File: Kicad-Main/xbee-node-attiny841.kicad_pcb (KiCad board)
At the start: 2 copper layers, 58.5 x 58.5 mm, 40 parts, among them P10 CONN_1, P11 CONN_1, P12 CONN_1, P13 CONN_1, P14 CONN_1, P15 CONN_1, P16 CONN_1, P17 CONN_1, P18 CONN_1, P19 CONN_1, P2 XBee Adaptor, P20 CONN_1, P3 Debug Adaptor, P7 CONN_1, P8 CONN_1, P9 CONN_1, Q2 MMBT3904, Q3 2N7002, U1 ATTINY841, U2 MAX952ESA, U3 TPS77033

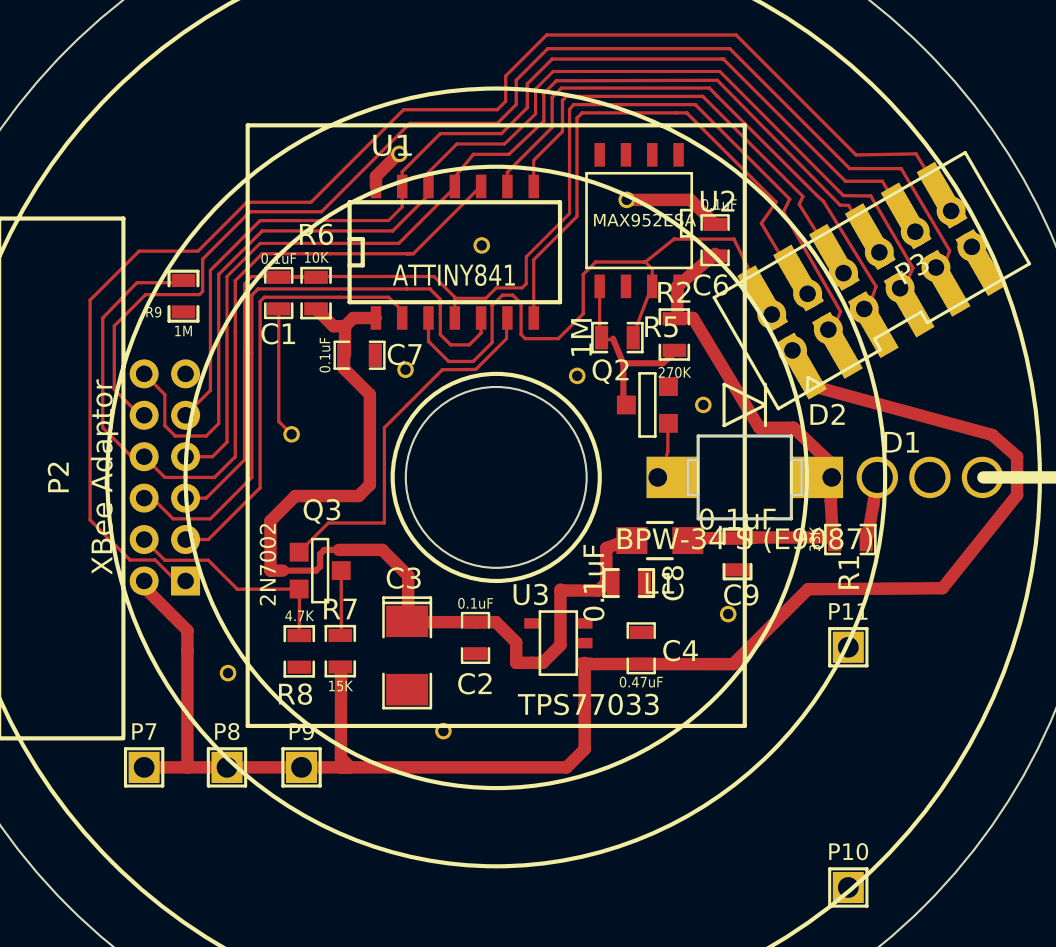
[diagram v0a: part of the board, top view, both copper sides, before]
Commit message: Update of Main PCB and generation of gerbers.
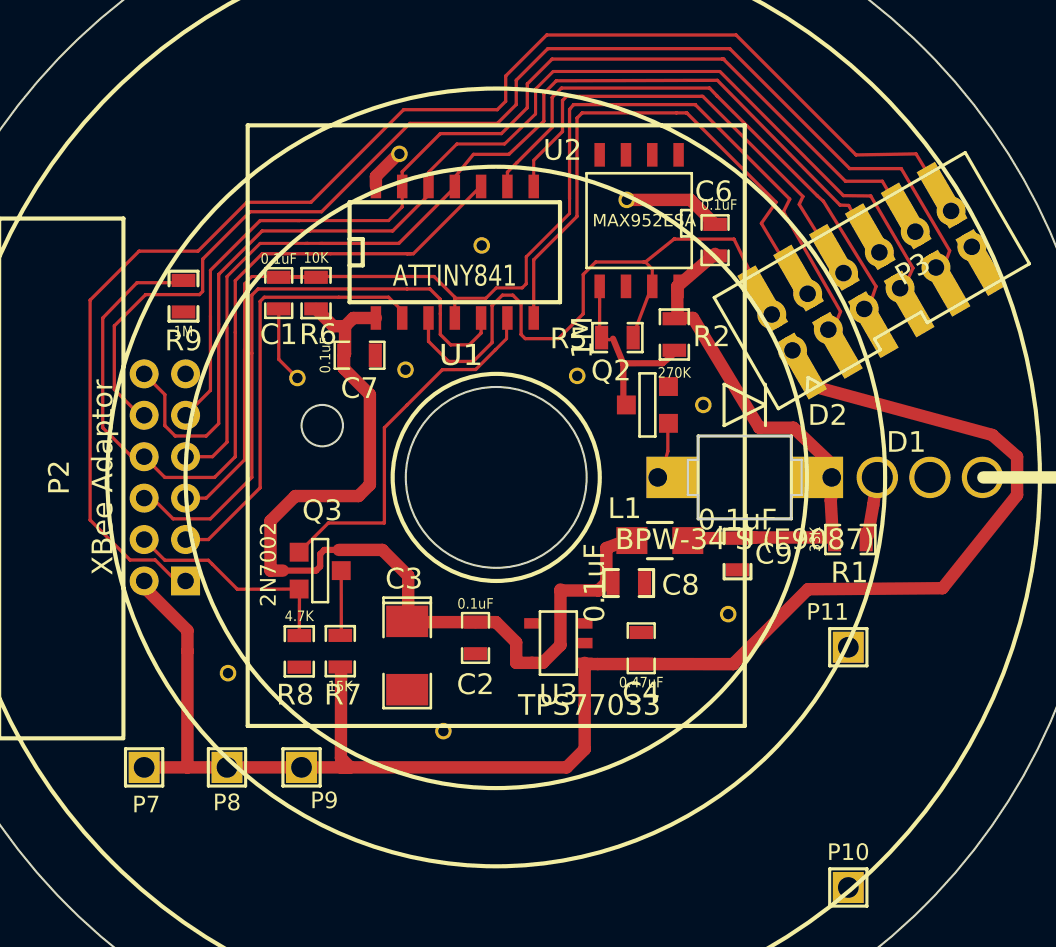
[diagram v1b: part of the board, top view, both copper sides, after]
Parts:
- moved P12 2.73 mm to (190.4, 95.2)
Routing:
- net GND: track 13.2 -> 10.6 mm
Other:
- outline, holes or cut-outs redrawn

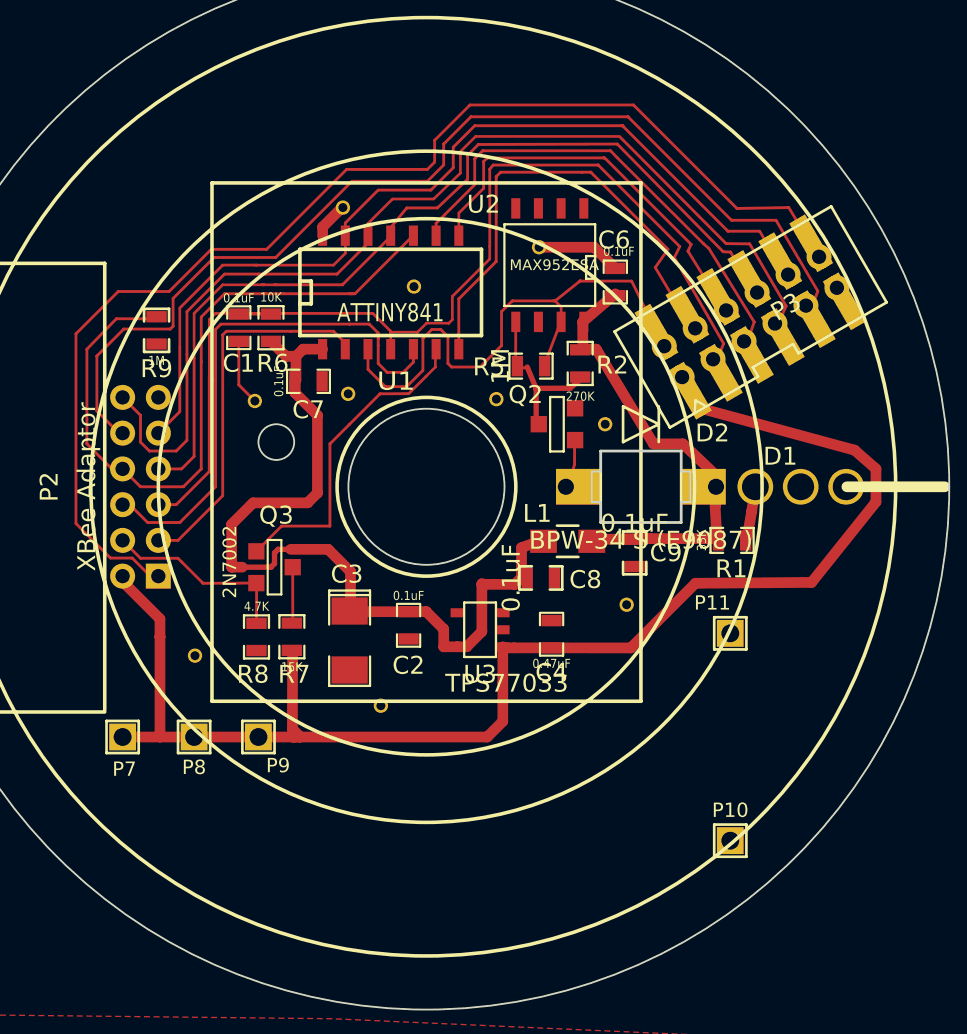
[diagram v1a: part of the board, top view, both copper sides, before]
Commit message: Update Main board PCB to modify battery monitor circuit.
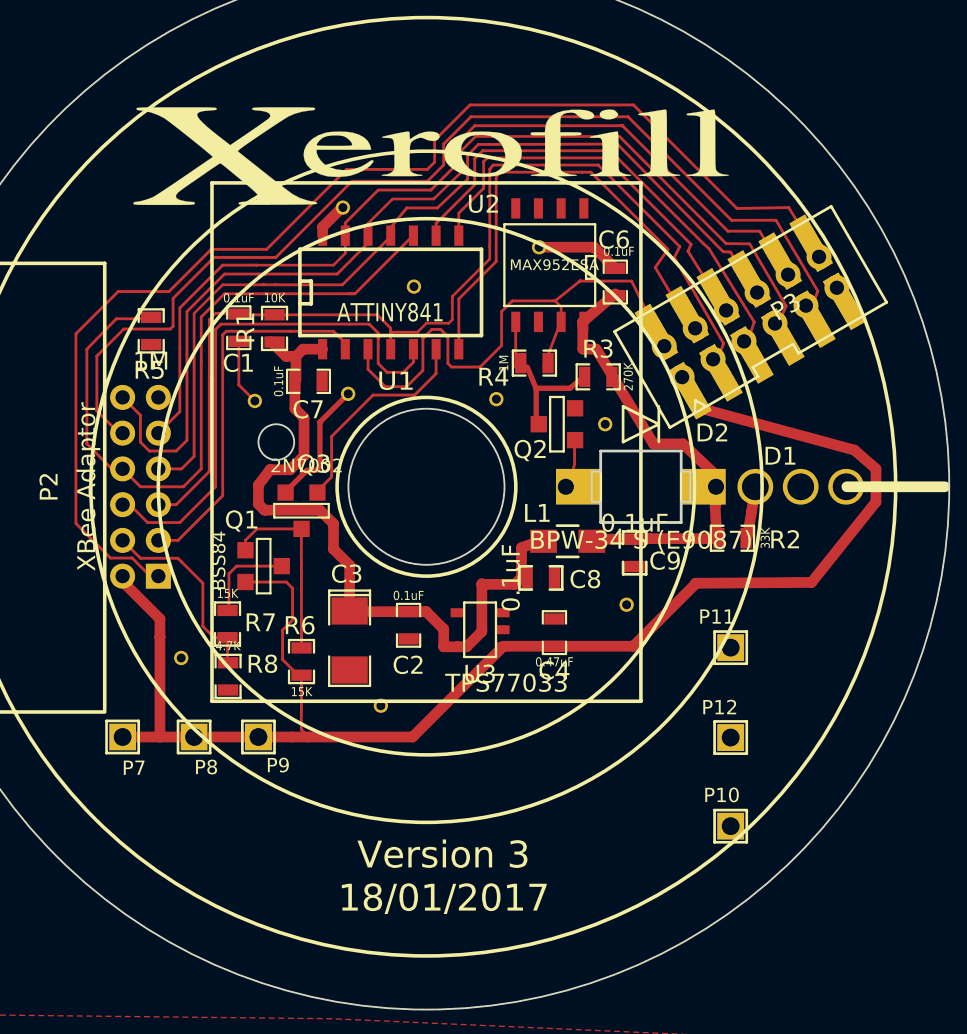
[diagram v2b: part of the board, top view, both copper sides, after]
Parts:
- removed R9: 1M, SMD_Packages:SMD-0603_r
- added G***: LOGO, PhotoDiode:Xerofill-Logo-Big, F.Cu at (200.2, 81.5)
- added P12: CONN_1, Connect:SIL-1, F.Cu at (217.0, 114.0)
- added Q1: BSS84, PhotoDiode:SOT23GDS, F.Cu at (190.9, 104.4)
- added R3: 270K, PhotoDiode:SM0603_Resistor, F.Cu at (209.6, 93.8)
- added R4: 1M, PhotoDiode:SM0603_Resistor, F.Cu at (206.0, 93.1)
- R1: value 33K -> 10K
- R2: value 270K -> 33K
- R6: value 10K -> 15K
- moved R1 28.2 mm to (191.5, 91.1), turned to 270 degrees
- moved R5 21.3 mm to (184.6, 91.3), turned to 90 degrees
- moved R6 18.8 mm to (193.0, 109.8), turned to 90 degrees
- moved R2 13.0 mm to (217.1, 102.9), turned to 0 degrees
- moved R7 3.67 mm to (188.9, 107.7), turned to 270 degrees
- moved Q3 3.50 mm to (193.0, 101.3), turned to 0 degrees
- moved R8 2.72 mm to (188.9, 110.6)
- moved P10 0.81 mm to (217.0, 119.0)
- moved P11 0.80 mm to (217.0, 109.0)
- moved P17 0.78 mm to (186.3, 109.6)
- moved C4 0.18 mm to (207.2, 108.2)
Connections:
- Q3 pad D: Net-(Q3-PadD) -> Net-(Q1-PadG)
- Q3 pad S: /VBatt -> GND
- R1 pad 1: /VDDA -> /Reset
- R1 pad 2: Net-(D1-Pad1) -> VDD
- R2 pad 2: Net-(Q2-Pad3) -> Net-(D1-Pad1)
- R5 pad 1: Net-(Q2-Pad3) -> GND
- R5 pad 2: /Count -> /Sleep-Rq
- R6 pad 1: /Reset -> /Battery
- R6 pad 2: VDD -> Net-(Q1-PadG)
- R7 pad 1: /Battery -> Net-(Q1-PadD)
- R7 pad 2: Net-(Q3-PadD) -> /VBatt
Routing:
- net Net-(Q1-PadG): track 0.00 -> 10.7 mm
- net GND: track 10.6 -> 17.9 mm
- net VDD: track 53.5 -> 47.0 mm
- net /PowerControl: track 18.1 -> 11.9 mm
- net Net-(Q1-PadD): track 0.00 -> 5.22 mm
- net Net-(Q3-PadD): track 3.25 -> 0.00 mm
- net /Reset: track 59.5 -> 57.9 mm
- net /Battery: track 85.6 -> 86.9 mm
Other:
- board text added: "Version 3 18/01/2017"

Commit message: Kicad-Main, Kicad-Mounts and Kicad-Testboard. Add a range of symbol and footprint libraries and repair some problems apparently due to randomized changes in Kicad repository libraries.
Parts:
- L1: value INDUCTOR_SMALL -> 100nH
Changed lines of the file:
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@@
     (links 99)
     (no_connects 4)
-    (area 162.31 68.7 242.200001 132.330001)
+    (area 170.699999 70.699999 229.300001 129.300001)
     (thickness 1.6)
     (drawings 29)
@@
   )
   (setup
-    (last_trace_width 0.3)
+    (last_trace_width 0.16)
     (user_trace_width 0.3)
     (user_trace_width 0.6)
@@
       (effects (font (size 1 1) (thickness 0.15)))
     )
-    (fp_text value INDUCTOR_SMALL (at 0 2.1 180) (layer F.Fab)
+    (fp_text value 100nH (at 0 2.1 180) (layer F.Fab)
       (effects (font (size 1 1) (thickness 0.15)))
     )
@@
   (segment (start 186.2 102) (end 184.4 102) (width 0.16) (layer F.Cu) (net 8))
   (segment (start 188.2 100) (end 186.2 102) (width 0.16) (layer F.Cu) (net 8))
-  (segment (start 192.121 100.324) (end 192.121 100.269) (width 0.3) (layer F.Cu) (net 9) (status C00000))
-  (segment (start 192.121 100.269) (end 193.31 99.08) (width 0.3) (layer F.Cu) (net 9) (status 400000))
+  (segment (start 193.82 99.08) (end 194.04 98.86) (width 0.3) (layer F.Cu) (net 9))
   (segment (start 193.31 99.08) (end 193.82 99.08) (width 0.3) (layer F.Cu) (net 9))
-  (segment (start 193.82 99.08) (end 194.04 98.86) (width 0.3) (layer F.Cu) (net 9))
+  (segment (start 192.121 100.324) (end 192.121 100.269) (width 0.3) (layer F.Cu) (net 9))
+  (segment (start 192.121 100.269) (end 193.31 99.08) (width 0.3) (layer F.Cu) (net 9))
   (segment (start 194.04 98.86) (end 194.04 96.38) (width 0.3) (layer F.Cu) (net 9))
-  (segment (start 194.04 96.38) (end 195.62 94.8) (width 0.3) (layer F.Cu) (net 9) (status 800000))
+  (segment (start 194.04 96.38) (end 195.62 94.8) (width 0.3) (layer F.Cu) (net 9))
   (segment (start 189.5 91.862) (end 189.5 94.3) (width 0.16) (layer F.Cu) (net 9))
   (segment (start 189.5 94.3) (end 190.4 95.2) (width 0.16) (layer F.Cu) (net 9))
@@
   (segment (start 194.19 85.464) (end 194.19 85.952) (width 0.6) (layer F.Cu) (net 9))
   (segment (start 194.19 85.952) (end 194.148 85.952) (width 0.15) (layer F.Cu) (net 9))
-  (segment (start 192.638 94.1) (end 192.638 95.628) (width 0.6) (layer F.Cu) (net 12) (status 400000))
+  (segment (start 192.638 94.1) (end 192.638 95.628) (width 0.6) (layer F.Cu) (net 12))
   (segment (start 192.37 99.05) (end 191.248125 99.05) (width 0.6) (layer F.Cu) (net 12))
   (segment (start 193.15 98.27) (end 192.37 99.05) (width 0.6) (layer F.Cu) (net 12))

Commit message: Minor tweaks on the PCBs ready to manufacture
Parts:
- added R9: 1M, PhotoDiode:SM0603_Resistor, F.Cu at (194.3, 96.5)
- moved P12 1.04 mm to (190.1, 94.2)
- moved P15 0.80 mm to (195.7, 94.0)
- moved P10 0.11 mm to (217.0, 119.1)
- moved P11 0.10 mm to (217.0, 108.9)
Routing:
- net /VDDA: track 30.3 -> 33.7 mm

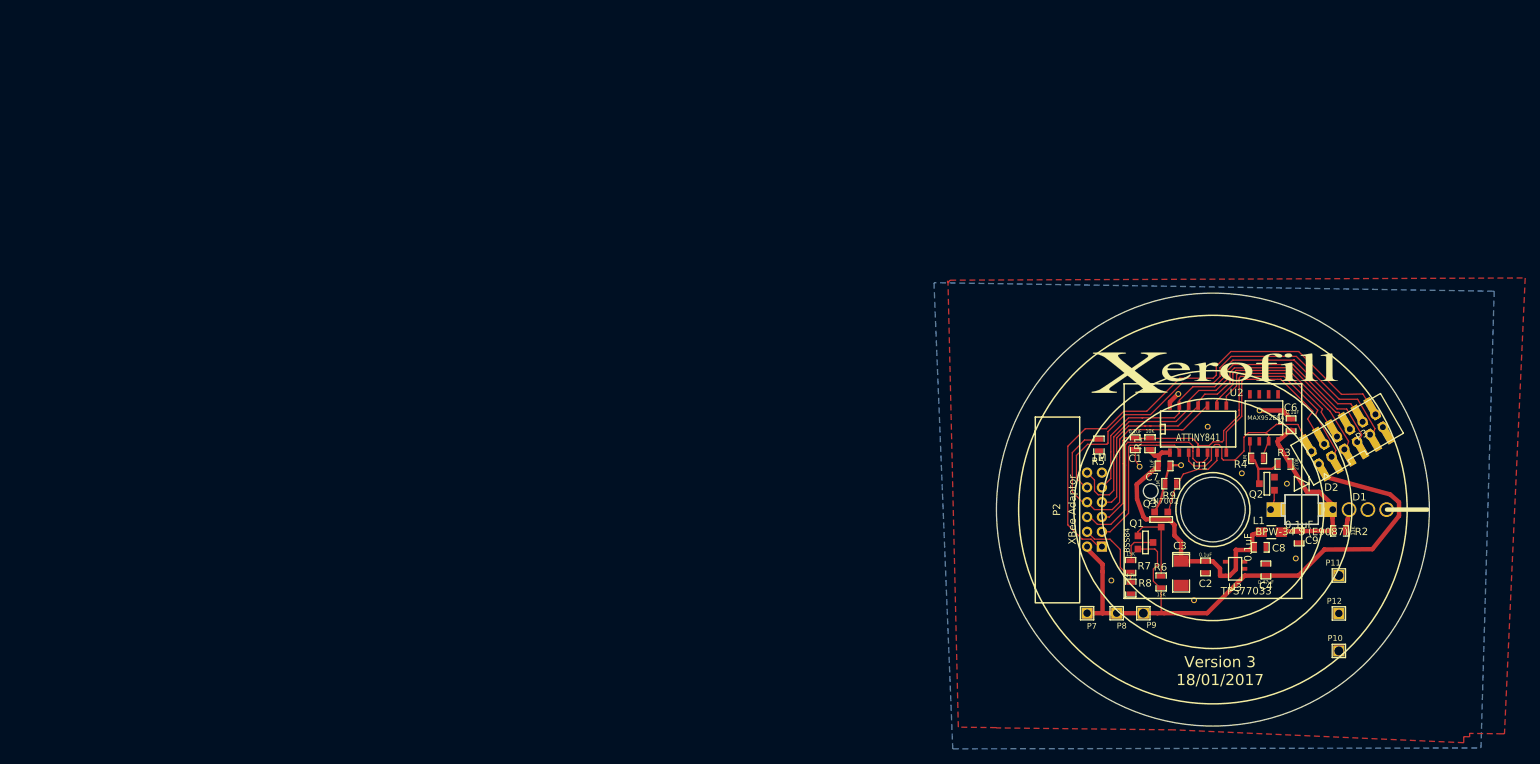
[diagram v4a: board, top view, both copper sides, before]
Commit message: Resolve issue between old version of CAM350 (9.5) and latest gerber format 4.6 where circles were not rendered correctly.
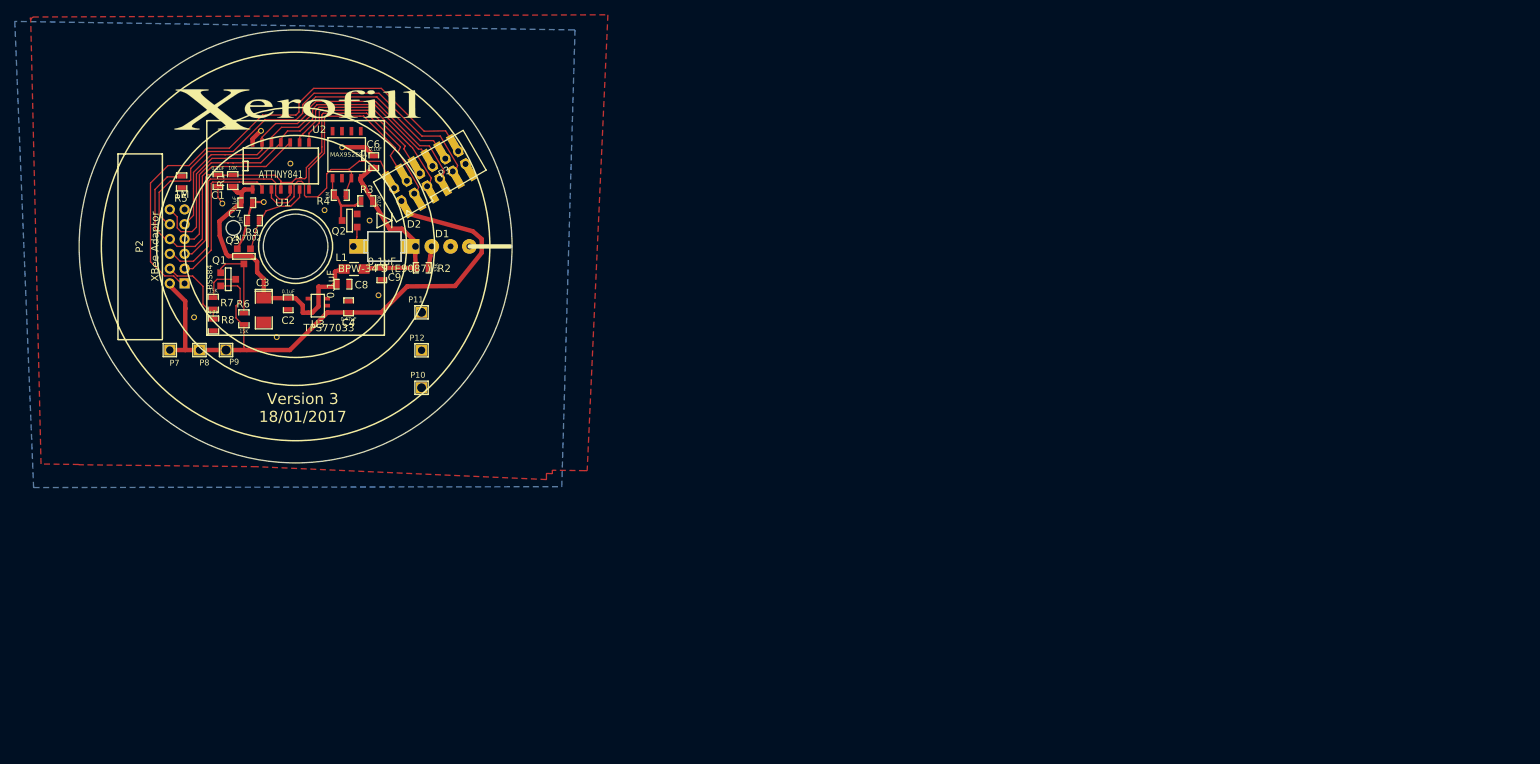
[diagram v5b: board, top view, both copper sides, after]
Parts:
- moved C7 129.0 mm to (69.4, 58.5)
- moved C8 129.0 mm to (82.4, 69.5)
- moved C9 129.0 mm to (87.7, 68.1)
- moved D1 129.0 mm to (94.4, 64.4)
- moved L1 129.0 mm to (83.9, 67.5)
- moved P10 129.0 mm to (93.1, 83.5)
- moved P11 129.0 mm to (93.1, 73.3)
- moved P12 129.0 mm to (93.1, 78.5)
- moved P13 129.0 mm to (75.3, 53.2)
- moved P18 129.0 mm to (82.3, 51.0)
- moved P20 129.0 mm to (80.0, 59.5)
- moved Q2 129.0 mm to (83.3, 60.9)
- moved R3 129.0 mm to (85.7, 58.3)
- moved R8 129.0 mm to (64.9, 75.0)
- moved R9 129.0 mm to (70.3, 60.9)
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
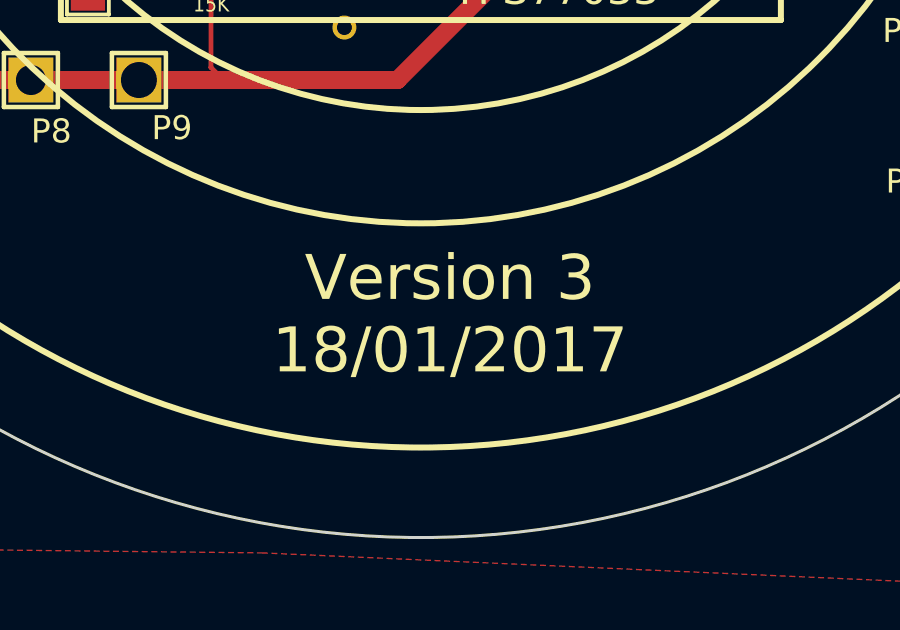
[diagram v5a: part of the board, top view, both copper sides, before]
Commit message: Kicad-Main: Regenerate gerbers with smaller LED mount holes.
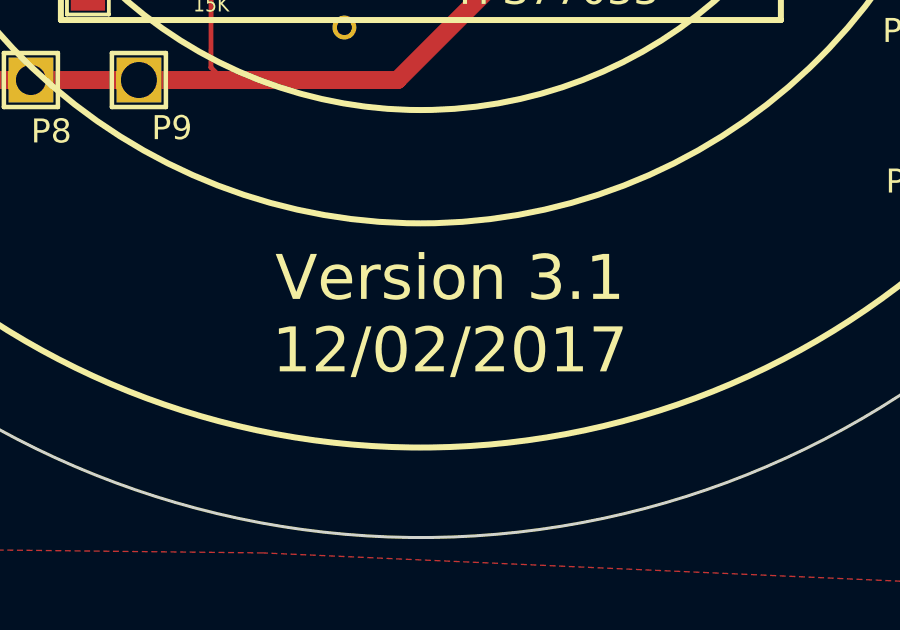
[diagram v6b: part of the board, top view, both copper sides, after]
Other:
- board text added: "Version 3.1 12/02/2017"
- board text removed: "Version 3 18/01/2017"
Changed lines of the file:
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@@
     (35 F.Paste user hide)
     (36 B.SilkS user hide)
-    (37 F.SilkS user hide)
-    (38 B.Mask user)
+    (37 F.SilkS user)
+    (38 B.Mask user hide)
     (39 F.Mask user)
     (40 Dwgs.User user hide)
@@
     )
   )
-  (gr_text "Version 3\n18/01/2017" (at 77.018 86.25) (layer F.SilkS)
+  (gr_text "Version 3.1\n12/02/2017" (at 77.018 86.25) (layer F.SilkS)
     (effects (font (size 1.5 1.5) (thickness 0.3)))
   )
